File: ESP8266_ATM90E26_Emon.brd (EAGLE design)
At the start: 50.8 x 50.8 mm, 96 parts, among them IC1 CP2104, IC2 RTC_PCF8523T, J2 ST-PJ-312, J4 12V AC, Q1 mmbt2222, Q2 mmbt2222, Q3 8.192MHz, SW2 KMR2, U1 ATM90E26, U2 SPX3819, U3 MCP73831T-2ACI/OT, U4 CJT1117-5.0-SOT223, X1 JSTPH, X2 ESP-12, X3 microsd, X4 20329, Y1 32khz

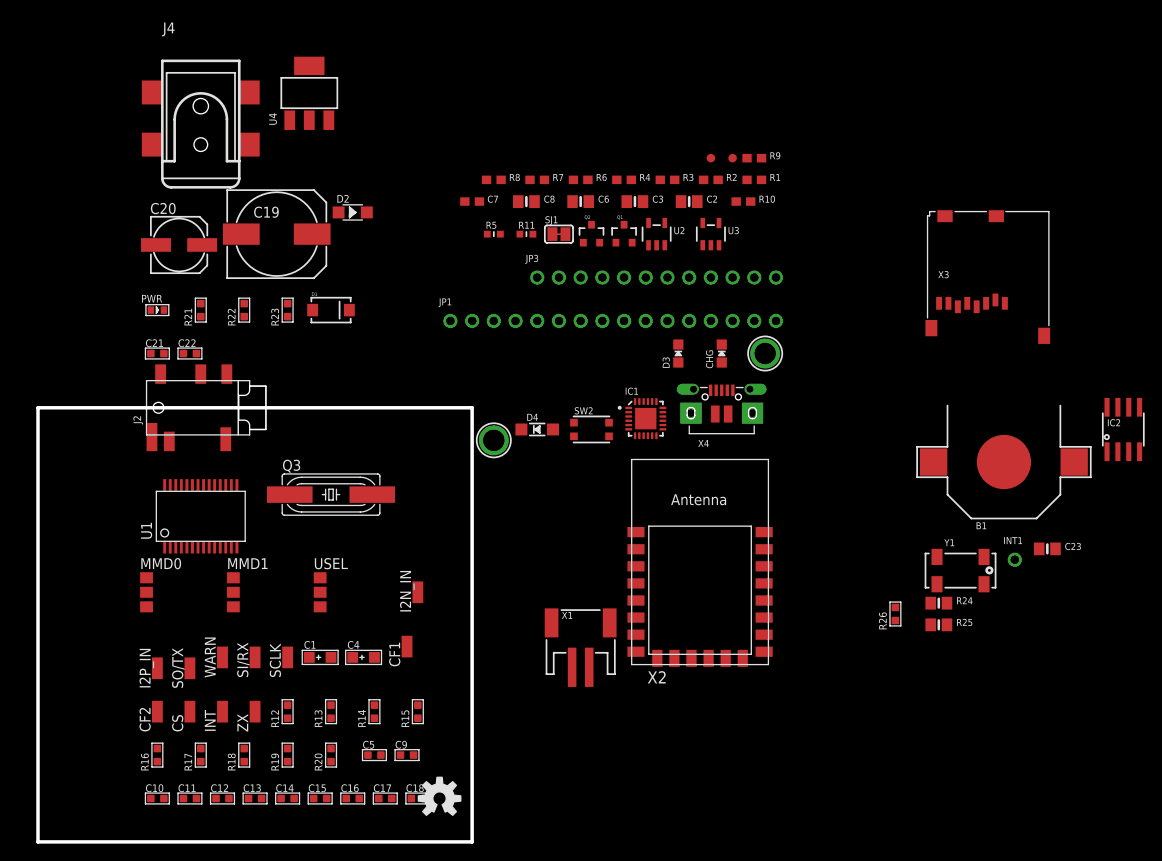
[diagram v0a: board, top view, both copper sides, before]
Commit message: Pulled parts into 50x50mm dimension
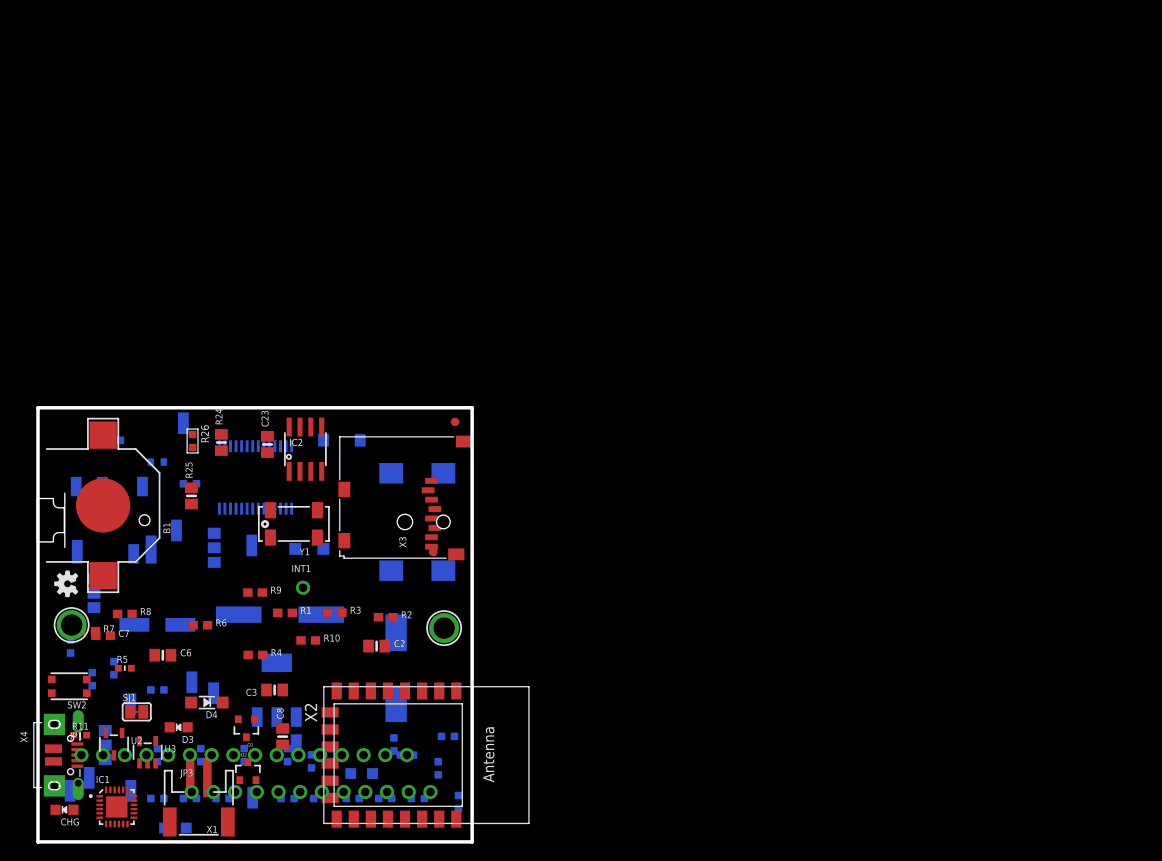
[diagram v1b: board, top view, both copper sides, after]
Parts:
- LOGO1: value OSHW-LOGOM -> OSHW-LOGOS; device SparkFun-Aesthetics:OSHW-LOGO-M -> SparkFun-Aesthetics:OSHW-LOGO-S
- moved B1 105.5 mm to (7.62, 39.4), turned to 90 degrees
- moved IC2 95.7 mm to (31.3, 45.9)
- moved CHG 93.6 mm to (3.10, 3.76), turned to 90 degrees
- moved C23 92.1 mm to (26.8, 46.5), turned to 90 degrees
- moved U3 89.6 mm to (12.8, 10.5)
- moved R25 88.7 mm to (18.0, 40.5), turned to 90 degrees
- moved U2 87.2 mm to (8.89, 11.4)
- moved X4 87.0 mm to (3.81, 10.2), turned to 270 degrees
- moved R24 86.0 mm to (21.5, 46.7), turned to 90 degrees
- moved R26 84.7 mm to (18.1, 46.9), turned to 180 degrees
- moved INT1 83.4 mm to (31.0, 29.7)
- moved X3 79.7 mm to (35.4, 33.2), turned to 90 degrees
- moved R11 78.5 mm to (4.93, 12.5)
- moved Y1 78.2 mm to (29.9, 37.2), turned to 180 degrees
- moved R9 77.4 mm to (25.4, 29.2)
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
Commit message: Some signal renaming
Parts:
- C2, C23, C3, C6, C8, R24, R25: device microbuilder:0805-NO -> microbuilder:0603-NO
- CHG: device microbuilder:CHIPLED_0805_NOOUTLINE -> microbuilder:CHIPLED_0603_NOOUTLINE
- INT1: device microbuilder:1X01_ROUND -> microbuilder:1X01_SMD_MASKHELD_1X2MM
- moved LOGO1 61.1 mm to (64.4, 26.4)
- moved U$35 55.1 mm to (1.80, 1.40)
- moved JP1 53.5 mm to (73.7, 30.5)
- moved JP3 43.9 mm to (72.6, 22.4)
- moved SW2 41.9 mm to (44.3, 28.4)
- moved J4 39.4 mm to (5.84, 37.4), flipped to the top
- moved R5 38.3 mm to (48.3, 24.1)
- moved R7 30.5 mm to (36.3, 25.9)
- moved C7 28.2 mm to (35.6, 27.9)
- moved R26 28.0 mm to (22.9, 19.4), turned to 270 degrees
- moved INT1 24.3 mm to (14.7, 47.7), turned to 180 degrees
- moved R24 22.8 mm to (38.4, 31.4), turned to 180 degrees
- moved U$31 22.1 mm to (3.17, 47.5)
- moved U$32 21.8 mm to (47.5, 3.17)
- moved R25 21.6 mm to (38.3, 33.2), turned to 180 degrees
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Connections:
- removed net +3V3: C1.+, C23.1, C9.1, IC2.8, MMD0.1, MMD1.3, R12.2, R24.2, R25.2, U1.3, U1.4, USEL.1, X3.4
- removed net N$9: MMD1.2, U1.1
- removed net USB: D2.-, R23.1
- net 3.3V: now also C1.+, C23.1, C9.1, IC2.8, MMD0.1, MMD1.2, MMD1.3, R12.2, R24.2, R25.2, U1.1, U1.3, U1.4, USEL.1, X3.4
- net INT1: now also INT1.P$1; no longer INT1.1
- net VBUS: now also D2.-, R23.1

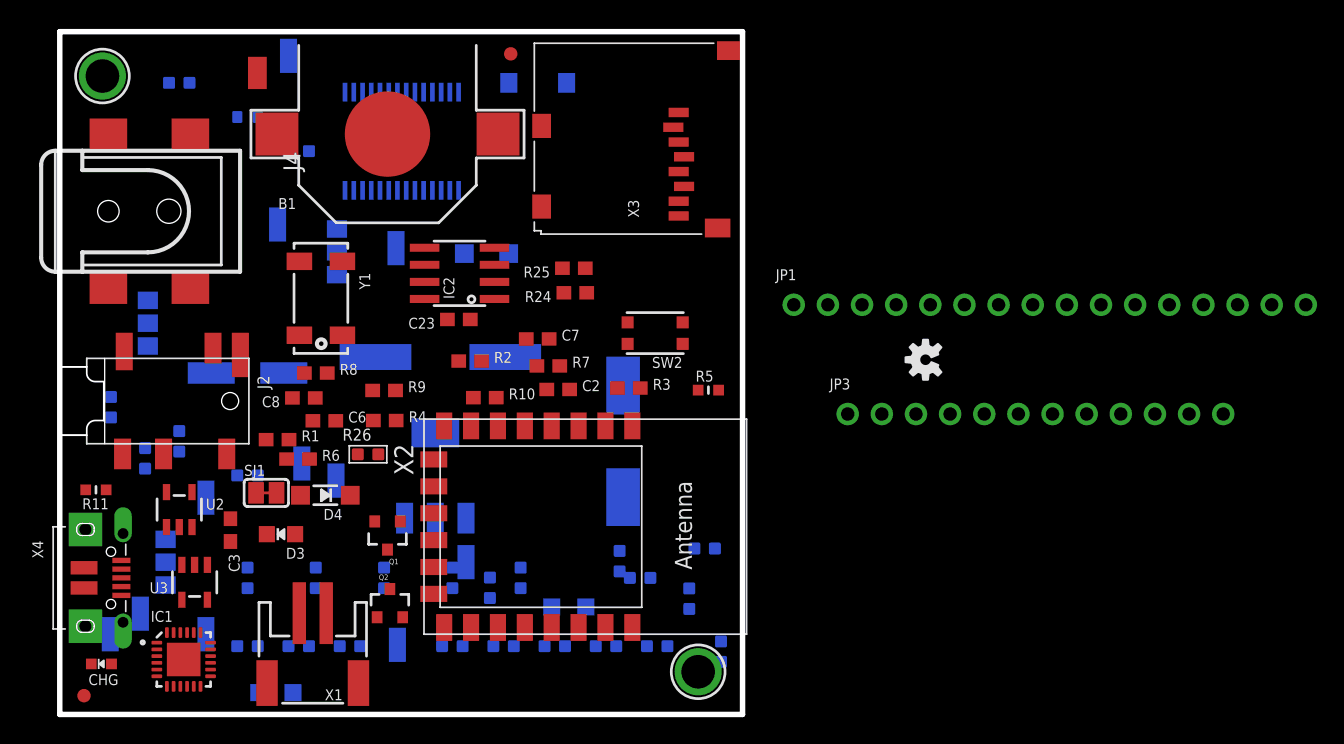
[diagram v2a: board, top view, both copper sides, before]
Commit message: Squeeze all parts into 50x50mm
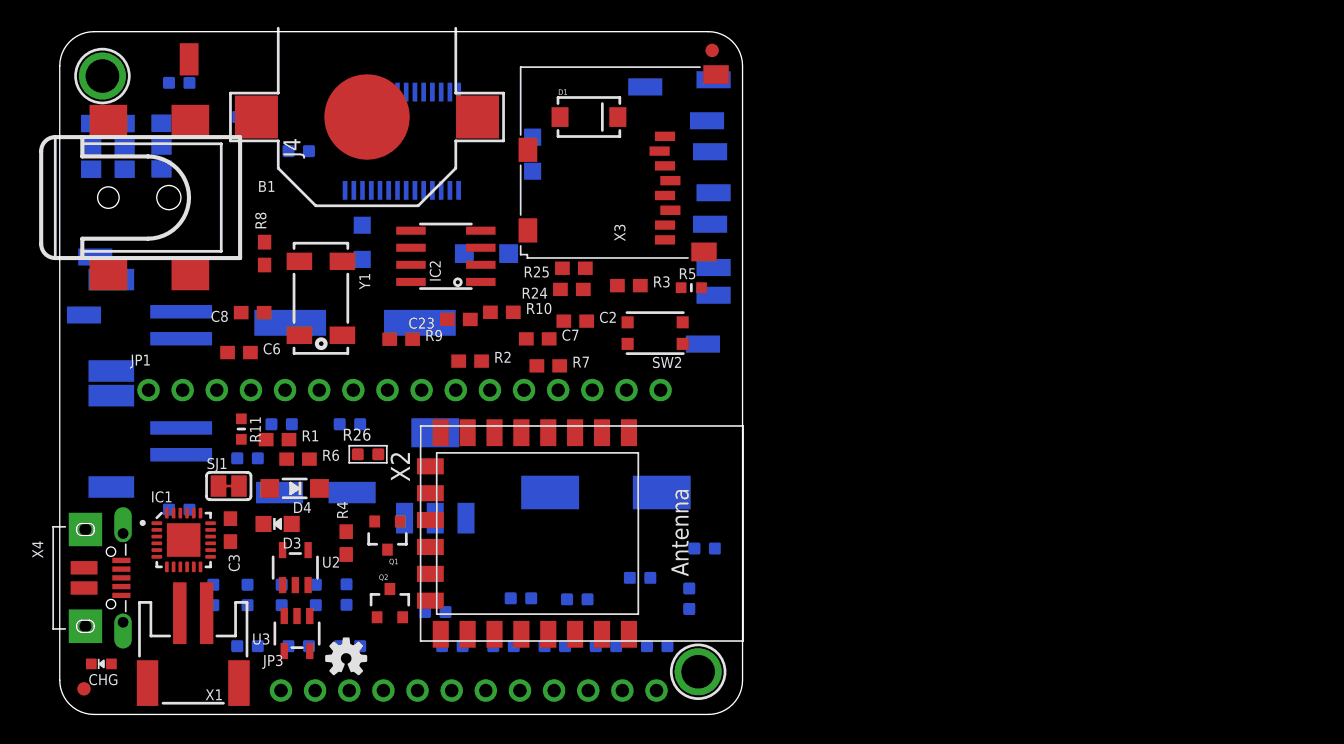
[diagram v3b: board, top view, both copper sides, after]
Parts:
- removed J2: ST-PJ-312, Seeed-OPL-Connector:AUDIO6P-SMD-3.5-14.0X6.4X5.0MM
- added J1, J3: (no value), SparkFun-Connectors:JST-2-SMD
- moved CF2 57.3 mm to (48.4, 41.9), turned to 270 degrees
- moved SCLK 51.4 mm to (48.4, 36.5), turned to 270 degrees
- moved LOGO1 48.5 mm to (21.3, 4.17), turned to 0 degrees
- moved JP1 48.4 mm to (25.7, 24.1)
- moved JP3 46.9 mm to (30.4, 1.78)
- moved CS 45.4 mm to (48.6, 31.2), turned to 270 degrees
- moved CF1 45.3 mm to (48.2, 44.2), turned to 270 degrees
- moved SO/TX 44.1 mm to (48.6, 38.8), turned to 270 degrees
- moved INT 41.0 mm to (48.6, 47.2), turned to 270 degrees
- moved I2N_IN 35.7 mm to (2.64, 34.0), turned to 270 degrees
- moved C1 34.1 mm to (22.5, 35.1), turned to 270 degrees
- moved WARN 33.9 mm to (48.6, 33.2), turned to 270 degrees
- moved C4 33.8 mm to (35.2, 41.7), turned to 270 degrees
- moved USEL 31.1 mm to (4.83, 42.3), turned to 180 degrees
- moved ZX 29.2 mm to (43.6, 46.7), turned to 270 degrees
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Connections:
- net I1N_IN1: now also J1.1; no longer J2.COM1
- net I1P_IN1: now also J1.2; no longer J2.L
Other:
- outline, holes or cut-outs redrawn
